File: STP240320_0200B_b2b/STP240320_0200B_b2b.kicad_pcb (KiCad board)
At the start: 2 copper layers, 6.1 x 11.2 mm, 2 parts, among them J1 Conn_02x08_Odd_Even

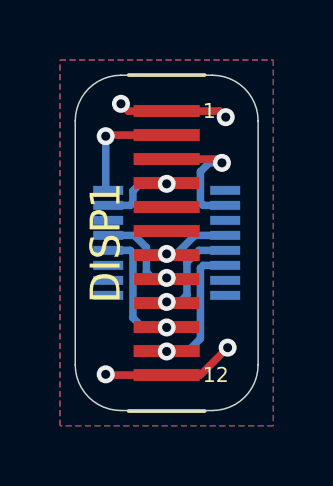
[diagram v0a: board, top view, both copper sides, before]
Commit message: kicad: update to kicad 6
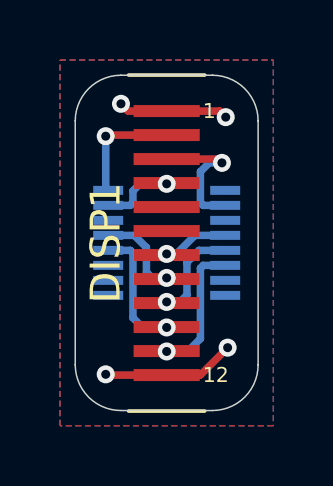
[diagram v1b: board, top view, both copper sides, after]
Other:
- net class Default removed

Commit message: ci: add CI (#1)
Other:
- board text added: "${TAG}"
- board text added: "(${REVISION})"
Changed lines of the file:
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@@
     )
   )
+  (property "DATE" "YYYY-MM-DD HH:MM:SS")
+  (property "REVISION" "REVISION")
+  (property "TAG" "TAG")
   (net 0 "")
   (net 1 "GND")
@@
     (at 116.332 83.9978)
     (attr through_hole)
-    (fp_text reference "DISP1" (at -2.032 4.3942 90) (layer "F.SilkS")
-      (effects (font (size 1 1) (thickness 0.15)))
+    (fp_text reference "DISP1" (at 1.651 4.3942 270) (layer "F.SilkS")
+      (effects (font (size 0.5 0.5) (thickness 0.1)))
     )
     (fp_text value "STP240320_0200B" (at -4.064 3.8862 90) (layer "F.Fab")
@@
   (gr_line (start 119.38 92.456) (end 119.38 84.328) (layer "Edge.Cuts") (width 0.05))
   (gr_arc (start 113.284 84.328) (mid 113.730369 83.250369) (end 114.808 82.804) (layer "Edge.Cuts") (width 0.05))
+  (gr_text "${TAG}" (at 114.3 86.741 90) (layer "F.SilkS")
+    (effects (font (size 0.5 0.5) (thickness 0.1)))
+  )
+  (gr_text "(${REVISION})" (at 114.3 90.424 90) (layer "F.SilkS")
+    (effects (font (size 0.5 0.5) (thickness 0.1)))
+  )
   (segment (start 116.332 83.9978) (end 118.0973 83.9978) (width 0.25) (layer "F.Cu") (net 1))
   (segment (start 115.0493 83.9978) (end 114.808 83.7565) (width 0.25) (layer "F.Cu") (net 1))

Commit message: b2b: default thickness is 0.8mm
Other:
- board text added: "Recommended PCB thickness: 0.8mm"
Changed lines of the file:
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@@
 (kicad_pcb (version 20211014) (generator pcbnew)
   (general
-    (thickness 1.6)
+    (thickness 0.8)
   )
   (paper "A4")
@@
   )
   (setup
+    (stackup
+      (layer "F.SilkS" (type "Top Silk Screen"))
+      (layer "F.Paste" (type "Top Solder Paste"))
+      (layer "F.Mask" (type "Top Solder Mask") (thickness 0.01))
+      (layer "F.Cu" (type "copper") (thickness 0.035))
+      (layer "dielectric 1" (type "core") (thickness 0.71) (material "FR4") (epsilon_r 4.5) (loss_tangent 0.02))
+      (layer "B.Cu" (type "copper") (thickness 0.035))
+      (layer "B.Mask" (type "Bottom Solder Mask") (thickness 0.01))
+      (layer "B.Paste" (type "Bottom Solder Paste"))
+      (layer "B.SilkS" (type "Bottom Silk Screen"))
+      (copper_finish "None")
+      (dielectric_constraints no)
+    )
     (pad_to_mask_clearance 0.05)
     (pcbplotparams
@@
     (effects (font (size 0.5 0.5) (thickness 0.1)))
   )
+  (gr_text "Recommended PCB thickness: 0.8mm" (at 116.586 98.679) (layer "Cmts.User")
+    (effects (font (size 1 1) (thickness 0.15)))
+  )
   (segment (start 116.332 83.9978) (end 118.0973 83.9978) (width 0.25) (layer "F.Cu") (net 1))
